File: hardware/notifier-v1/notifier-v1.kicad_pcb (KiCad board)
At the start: 4 copper layers, 50 x 36 mm, 42 parts, among them J1 USB-C, J2 GC9A01, SW1 RESET, SW2 BOOT, SW3 BUTTON, U1 ESP32-S3-WROOM-1-N8R2, U2 USBLC6-2SC6, U3 TLV62569, U4 BME688, U5 SHT40-AD1B

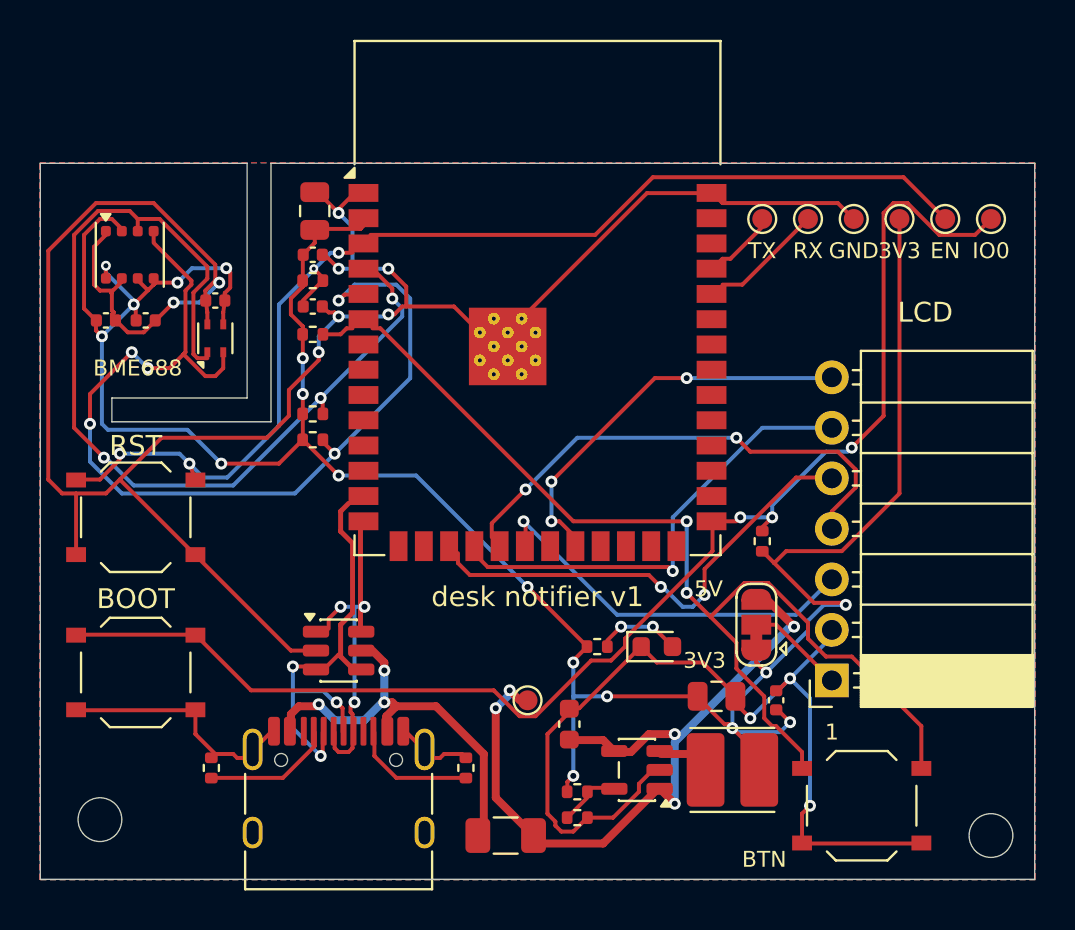
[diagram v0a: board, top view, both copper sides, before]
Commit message: Hardware: hierarchical, reviewable schematic (root block diagram + Power, MCU, Sensors, Display)
Real wires for coupled connections, explicit power symbols, notes and title blocks on every sheet.
Power nets are now GND/+3V3/VBUS/VBUS_IN/SW (no leading slash); router and layout patterns updated.

Co-Authored-By: Claude Opus 5.5 <noreply@anthropic.com>
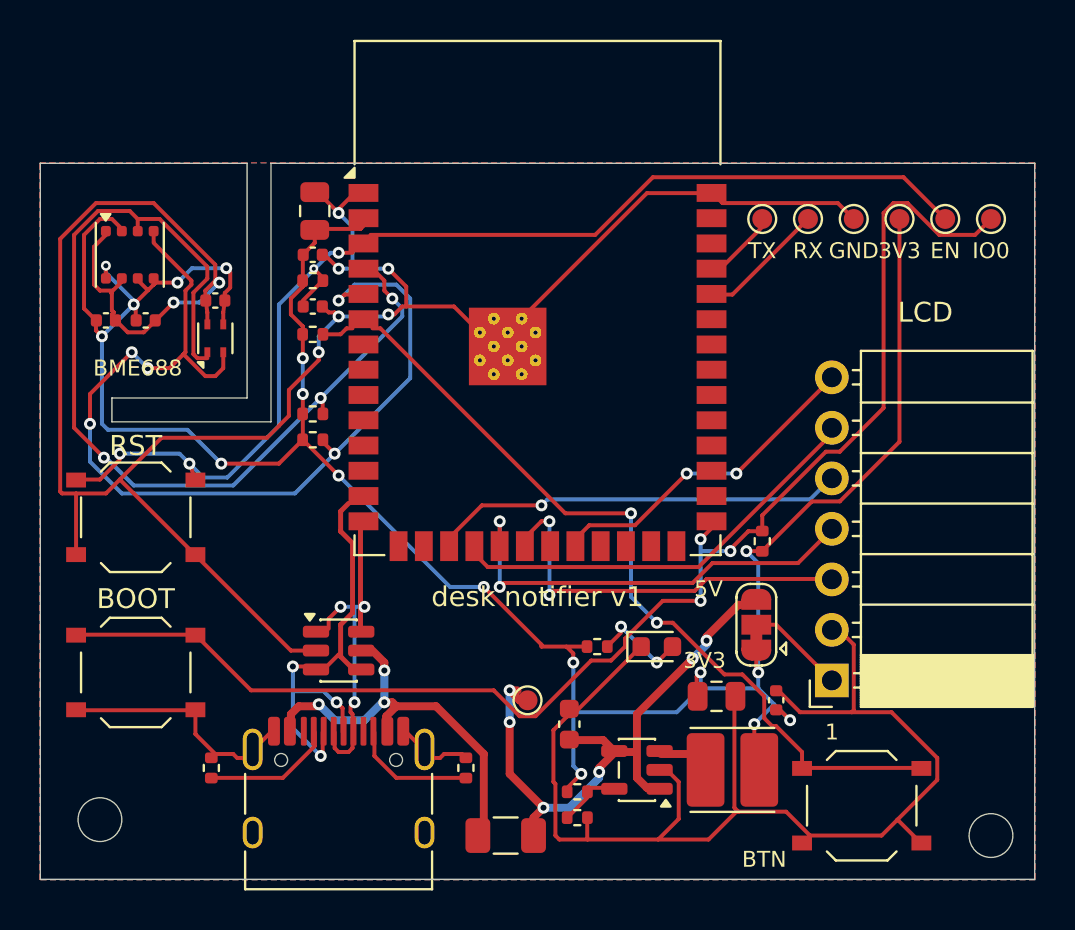
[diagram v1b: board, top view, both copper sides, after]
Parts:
- J1: value USB-C -> USB-C PWR/DATA
- J2: value GC9A01 -> GC9A01 DISPLAY
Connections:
- net /+3V3 renamed +3V3
- net /BOOT renamed /MCU/BOOT
- net /BTN renamed /MCU/BTN
- net /CC1 renamed /Power/CC1
- net /CC2 renamed /Power/CC2
- net /EN renamed /MCU/EN
- net /FB renamed /Power/FB
- net /GND renamed GND
- net /LCD_VCC renamed /Display/LCD_VCC
- net /LED_A renamed /Power/LED_A
- net /RXD0 renamed /MCU/RXD0
- net /SW renamed SW
- net /TXD0 renamed /MCU/TXD0
- net /VBUS renamed VBUS
- net /VBUS_IN renamed VBUS_IN
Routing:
- net GND: track 181.1 -> 195.9 mm, vias 11 -> 8
- net /MCU/BTN: track 53.3 -> 42.0 mm
- net VBUS: track 36.7 -> 31.6 mm, vias 5 -> 6
- net +3V3: track 135.4 -> 131.1 mm
- net /LCD_RST: track 19.8 -> 16.3 mm, vias 3 -> 2
- net /LCD_DC: track 23.6 -> 20.4 mm, vias 2 -> 1
- net /LCD_MOSI: track 24.9 -> 22.1 mm
- net /MCU/BOOT: track 67.0 -> 68.7 mm
- net /LCD_CS: track 22.7 -> 21.1 mm, vias 1 -> 0
- net /MCU/RXD0: track 5.67 -> 6.37 mm
- net /Power/LED_A: track 4.00 -> 4.67 mm
- net /LCD_SCLK: track 19.3 -> 19.5 mm, vias 1 -> 2
